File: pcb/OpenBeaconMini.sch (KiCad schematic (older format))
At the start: 47 parts, among them J1 *+12VDC, J2 *Ant, Q1 2N4401, Q2 2N4403, Q3 2N4401, Q4 2N7000, Q5 2N4401, U1 78L05, U2 ATTINY45-20PU, X1 CRYSTAL

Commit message: New OpenBeacon Mini for 2017
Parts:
- removed C13: 100n, symbol C
- removed C14, C15, C16: C, symbol C
- removed C2: 45, symbol CTRIM
- removed D1: Red, symbol LED
- removed J1: *+12VDC, symbol CONN_3
- removed J2: *Ant, symbol BNC
- removed L1: L, symbol L
- removed L3, L4: L-IRONCORE, symbol L-IRONCORE
- removed Q1, Q3, Q5: 2N4401, symbol NPN
- removed Q4: 2N7000, symbol MOSFET_N
- removed R11: 330, symbol R
- removed R12, R3: 150k, symbol R
- removed R13: 1k, symbol R
- removed R14: 4.7k, symbol R
- removed R15: 10, symbol R
- removed R16: 47, symbol R
- removed U1: 78L05, symbol VREG
- removed U2: ATTINY45-20PU, symbol ATTINY85
- removed X1: CRYSTAL, symbol CRYSTAL
- added C2: 100n, symbol C
- added J1: Bias V, symbol CONN_01X01
- added J2: PAI+, symbol CONN_01X01
- added J3: PAI-, symbol CONN_01X01
- added J4: Digital IO, symbol Conn_01x10
- added J5: SMA, symbol BNC
- added J6: I2C Bus, symbol Conn_01x04
- added J7: ADC Inputs, symbol Conn_01x10
- added J8: GND, symbol CONN_01X01
- added J9: BNC, symbol BNC
- added L1: FDSD0420-H-100M-P3, symbol L-IRONCORE
- added M1: LPFModule, symbol LPFModule
- added Q1: 2N7002, symbol MOS_N
- added Q3: RD00HVS1, symbol MOS_N
- added R3: PAT1220-C-10dB, symbol ChipAttenuator
- added S1: Left, symbol PUSHBUTTON_TACTILE
- added S2: Menu 1, symbol PUSHBUTTON_TACTILE
- added S3: Down, symbol PUSHBUTTON_TACTILE
- added S4: Up, symbol PUSHBUTTON_TACTILE
- added S5: Menu 2, symbol PUSHBUTTON_TACTILE
- added S6: Right, symbol PUSHBUTTON_TACTILE
- added S7: Back, symbol PUSHBUTTON_TACTILE
- added U1: TLV61046A, symbol TLV61046A
- added U2: ASTX-H11-25.000MHZ-T, symbol OSCILLATOR
- added U3: SN74LVC1G17, symbol SN74LVC1G17
- added U4: SI5351A, MODULE, symbol SI5351A
- added U5: MCP4725A1T-E/CH, symbol MCP4725A1T
- added U6: 128x32OLED, symbol 128x32OLED
- added U7: Empyrean, symbol Empyrean
- C1: value Gimmick -> 10n
- C3: value C -> 2.2u
- C4: value C -> 10u
- C7, C9: value 100n -> 1u
- L2: value FT37-43 10T -> FB2402-61 5T
- Q2: value 2N4403 -> MMBT4403
- R1, R2: value 10k -> 22k
- R10: value 22k -> 10k
- R4: value 47 -> 22k
- R5: value 2.2k -> 3.3k
- R6: value 150k -> 10
- R7: value 22k -> 56
- R8: value 1k -> 1 1%
- R9: value 150k -> 10k
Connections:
- net labels added: +3.3V, A1, A2, A3, A4, A5, BAND_ID, BTN_BACK, BTN_DOWN, BTN_DSP_1, BTN_DSP_2, BTN_LEFT, BTN_RIGHT, BTN_UP, CLK0, D10, D11, D7, D8, D9, SCL, SDA, TX
- net labels removed: +12V, FSK, Key, S1, S2, S3
- wire segments 88 -> 136
- no-connect marks 1 -> 8
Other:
- note added: "Boost Converter"
- note added: "Keying"
- note added: "Low-Pass Filter\nPlug-in Module"
- note added: "PA Bias"
- note added: "Power Amplifier"
- note added: "Si5351A PLL"
- note added: "User Interface"
- note removed: "Freq Trim"
- note removed: "Offset"
- note removed: "Starred components (*) are not included with kit"

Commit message: Add I2C level conversion
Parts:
- added J5: SMA, symbol BNC
- added Q4, Q5: 2N7002, symbol MOS_N
- added R10, R9: 10k, symbol R
- renumbered J9 to J10, J5 to J6, J6 to J7, J7 to J8, J8 to J9, R9 to R11, R10 to R12
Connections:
- net labels added: SCL_5V, SDA_5V
- wire segments 136 -> 146
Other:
- note added: "I2C Level Conversion"

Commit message: Add firmware to repo
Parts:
- C1, C10, C11, C12, C2, C3, C4, C5, C6, C7, C8, C9: footprint (none) -> EtherkitKicadLibrary:C_0805
- J1, J2, J3, J9: footprint (none) -> Measurement_Points:Measurement_Point_Square-TH_Small
- J10: footprint (none) -> EtherkitKicadLibrary:BNC-AMPHENOL-31-5431-10RFX
- J4, J8: footprint (none) -> Pin_Headers:Pin_Header_Straight_1x06_Pitch2.54mm; symbol Conn_01x10 -> Conn_01x06
- J5, J6: footprint (none) -> EtherkitKicadLibrary:SMA-ENDLAUNCH
- J7: footprint (none) -> Pin_Headers:Pin_Header_Straight_1x04_Pitch2.54mm
- L1: footprint (none) -> EtherkitKicadLibrary:Murata100M
- L2: footprint (none) -> EtherkitKicadLibrary:BN2402
- M1: footprint (none) -> EtherkitKicadLibrary:LPFModule
- Q1, Q4, Q5: footprint (none) -> EtherkitKicadLibrary:SOT23-2N7002
- Q2: footprint (none) -> EtherkitKicadLibrary:SOT23-MMBT440X
- Q3: footprint (none) -> EtherkitKicadLibrary:SOT89-3
- R1, R10, R11, R12, R2, R4, R5, R6, R7, R8, R9: footprint (none) -> EtherkitKicadLibrary:R_0805
- R3: footprint (none) -> EtherkitKicadLibrary:PAT1220
- S1, S2, S3, S4, S5, S6, S7: footprint (none) -> EtherkitKicadLibrary:Omron_B3F-1052
- U1, U5: footprint (none) -> EtherkitKicadLibrary:SOT23-6
- U2: footprint (none) -> EtherkitKicadLibrary:ASTX-H11-25.000MHZ-T
- U3: footprint (none) -> EtherkitKicadLibrary:SOT23-5
- U4: footprint MODULE -> EtherkitKicadLibrary:MSOP-10
- U6: footprint (none) -> EtherkitKicadLibrary:128x32OLED
- U7: footprint (none) -> EtherkitKicadLibrary:Empyrean
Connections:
- wire segments 146 -> 142

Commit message: New firmware and time sync software
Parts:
- R10, R11, R12, R9: value 10k -> 3.3k
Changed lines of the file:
@@
 Sheet 1 1
 Title "OpenBeacon Mini"
-Date "2017-12-02"
+Date "2018-04-10"
 Rev "A"
 Comp "Etherkit"
@@
 P 7500 4585
 F 0 "R12" H 7635 4625 50  0000 C CNN
-F 1 "10k" H 7630 4560 50  0000 C CNN
+F 1 "3.3k" H 7655 4555 50  0000 C CNN
 F 2 "EtherkitKicadLibrary:R_0805" H 7500 4585 60  0001 C CNN
 F 3 "" H 7500 4585 60  0000 C CNN
@@
 P 7180 4585
 F 0 "R11" H 7310 4625 50  0000 C CNN
-F 1 "10k" H 7315 4555 50  0000 C CNN
+F 1 "3.3k" H 7315 4555 50  0000 C CNN
 F 2 "EtherkitKicadLibrary:R_0805" H 7180 4585 60  0001 C CNN
 F 3 "" H 7180 4585 60  0000 C CNN
@@
 P 6090 5600
 F 0 "R10" H 6225 5645 50  0000 C CNN
-F 1 "10k" H 6225 5570 50  0000 C CNN
+F 1 "3.3k" H 6225 5570 50  0000 C CNN
 F 2 "EtherkitKicadLibrary:R_0805" H 6090 5600 60  0001 C CNN
 F 3 "" H 6090 5600 60  0000 C CNN
@@
 P 5790 5600
 F 0 "R9" H 5900 5640 50  0000 C CNN
-F 1 "10k" H 5925 5570 50  0000 C CNN
+F 1 "3.3k" H 5925 5570 50  0000 C CNN
 F 2 "EtherkitKicadLibrary:R_0805" H 5790 5600 60  0001 C CNN
 F 3 "" H 5790 5600 60  0000 C CNN

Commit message: Reimplement config storage, implement flash NVM
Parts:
- C1, C10, C11, C12, C2, C3, C4, C5, C6, C7, C8, C9: symbol C -> EtherkitKicadLibrary:C
- J1, J2, J3, J9: symbol CONN_01X01 -> EtherkitKicadLibrary:CONN_01X01
- J10, J5, J6: symbol BNC -> EtherkitKicadLibrary:BNC
- J4, J8: symbol Conn_01x06 -> OpenBeaconMini-rescue:Conn_01x06
- J7: symbol Conn_01x04 -> OpenBeaconMini-rescue:Conn_01x04
- L1, L2: symbol L-IRONCORE -> EtherkitKicadLibrary:L-IRONCORE
- M1: symbol LPFModule -> EtherkitKicadLibrary:LPFModule
- Q1, Q3, Q4, Q5: symbol MOS_N -> EtherkitKicadLibrary:MOS_N
- Q2: symbol PNP -> EtherkitKicadLibrary:PNP
- R1, R10, R11, R12, R2, R4, R5, R6, R7, R8, R9: symbol R -> EtherkitKicadLibrary:R
- R3: symbol ChipAttenuator -> EtherkitKicadLibrary:ChipAttenuator
- S1, S2, S3, S4, S5, S6, S7: symbol PUSHBUTTON_TACTILE -> EtherkitKicadLibrary:PUSHBUTTON_TACTILE
- U1: symbol TLV61046A -> EtherkitKicadLibrary:TLV61046A
- U2: symbol OSCILLATOR -> EtherkitKicadLibrary:OSCILLATOR
- U3: symbol SN74LVC1G17 -> EtherkitKicadLibrary:SN74LVC1G17
- U4: symbol SI5351A -> EtherkitKicadLibrary:SI5351A
- U5: symbol MCP4725A1T -> EtherkitKicadLibrary:MCP4725A1T
- U6: symbol 128x32OLED -> EtherkitKicadLibrary:128x32OLED
- U7: symbol Empyrean -> EtherkitKicadLibrary:Empyrean
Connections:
- wire segments 142 -> 188

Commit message: Initial schematic to Rev B
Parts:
- removed J4: Digital IO, Pin_Headers:Pin_Header_Straight_1x06_Pitch2.54mm, symbol OpenBeaconMini-rescue:Conn_01x06
- added C12, C13, C17: 100n, EtherkitKicadLibrary:C_0805, symbol EtherkitKicadLibrary:C
- added C15, C16: 4.7u, EtherkitKicadLibrary:C_0805, symbol EtherkitKicadLibrary:C
- added D1, D2: 1N4148W, Diode_SMD:D_SOD-123, symbol EtherkitKicadLibrary:DIODE
- added J10: UART, Pin_Headers:Pin_Header_Straight_1x04_Pitch2.54mm, symbol OpenBeaconMini-rescue:Conn_01x04
- added J4: Digital IO, Pin_Headers:Pin_Header_Straight_1x04_Pitch2.54mm, symbol OpenBeaconMini-rescue:Conn_01x04
- added K1, K2: G5V-1-DC5, Relay_THT:Relay_SPDT_Omron_G5V-1, symbol Relay:G5V-1
- added M2: LPF 2, EtherkitKicadLibrary:LPFModule, symbol EtherkitKicadLibrary:LPFModule
- added Q6: 2N7002, EtherkitKicadLibrary:SOT23-2N7002, symbol EtherkitKicadLibrary:MOS_N
- added R10, R9: 270k, EtherkitKicadLibrary:R_0805, symbol EtherkitKicadLibrary:R
- added R13: 22k, EtherkitKicadLibrary:R_0805, symbol EtherkitKicadLibrary:R
- added U8: 24AA64T, Package_TO_SOT_SMD:SOT-23-5, symbol EtherkitKicadLibrary:24AA64T
- M1: value LPFModule -> LPF 1
- Q3: value RD00HVS1 -> 2SK3074
- renumbered C2 to C1, C12 to C14, C3 to C2, C4 to C3, C1 to C4, J10 to J11, J8 to J5, J5 to J6, J6 to J7, J7 to J8, R9 to R11, R10 to R12, R11 to R14, R12 to R15, R4 to R2, R2 to R3, R3 to R4, S2 to S1, S5 to S2, S1 to S3, S3 to S4, S4 to S5, S7 to S6, S6 to S7
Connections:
- net BAND_ID is gone; now on net BAND_ID_1: U7.8 (A0)
- net D7 is gone; now on net BTN_LEFT: U7.21 (D7)
- net D8 is gone; now on net BTN_DSP_1: U7.22 (D8)
- net D9 is gone; now on net BTN_DSP_2: U7.23 (D9)
- net +3.3V: now also M1.9 (VCC), C15.1, C16.1, C17.1, J10.1 (Pin_1), M2.9 (VCC), U8.4 (VCC); no longer M1.8 (GND)
- net +5V: now also D1.2 (K), D2.2 (K), K1.2, K2.2
- net A2: now also J5.1 (Pin_1); no longer J5.3 (Pin_3)
- net A3: now also J5.3 (Pin_3); no longer J5.5 (Pin_5)
- net A4: now also J5.5 (Pin_5)
- net BTN_DSP_1: no longer U7.14 (D0)
- net BTN_DSP_2: no longer U7.15 (D1)
- net BTN_LEFT: no longer U7.18 (D4)
- net D10: now also J4.3 (Pin_3)
- net GND: now also M1.1 (GND), M1.3 (GND), M1.5 (GND), M1.8 (GND), C12.2, C13.2, C15.2, C16.2, C17.2, J10.4 (Pin_4), J4.2 (Pin_2), J4.4 (Pin_4), M2.1 (GND), M2.3 (GND), M2.5 (GND), M2.6 (GND), M2.8 (GND), Q6.1 (S), R10.2, R13.2, R9.2, U8.2 (VSS), U8.5 (WP); no longer M1.9 (VCC)
- net SCL: now also U8.1 (SCL)
- net SDA: now also U8.3 (SDA)
- net TX: now also U7.26 (D12); no longer U7.27 (D13)
- net at C11.1: now also K1.5, K1.6
- net BAND_ID_1: now reaches M1.2 (BAND_V)
- net BAND_ID_1: now also C12.1, R9.1
- net at M1.4 (RF): now also K1.1
- net at M1.7 (RF): now also K2.1; no longer J11.1 (In)
- net at C3.1, Q2.1 (E), U1.5 (VO): now also R2.1; no longer C4.1
- net at Q2.3 (C), R6.2: now also C4.1; no longer R2.1
- net A1 renamed BAND_ID_2
- net BAND_ID_2: now also C13.1, M2.2 (BAND_V), R10.1; no longer J5.1 (Pin_1)
- net A5: no longer names the net of U7.13 (A5)
- net D11 renamed BAND_SW
- net BAND_SW: now also Q6.2 (G), R13.1
- new net: J11.1 (In), K2.5, K2.6
- new net: K1.10, M2.4 (RF)
- new net: K2.10, M2.7 (RF)
- new net BAND_RELAY: D1.1 (A), D2.1 (A), K1.9, K2.9, Q6.3 (D)
- new net D4: J4.1 (Pin_1), U7.18 (D4)
- new net UART_RX: J10.2 (Pin_2), U7.14 (D0)
- new net UART_TX: J10.3 (Pin_3), U7.15 (D1)
- no-connect marks 8 -> 9
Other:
- note added: "External EEPROM"
- note added: "IO Headers"
- note added: "Low-Pass Filter\nPlug-in Modules"
- note removed: "Low-Pass Filter\nPlug-in Module"
- moved on the sheet: C4, J11, J5, J8, M1, Q4, Q5, R11, R12, R14, R15, R2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

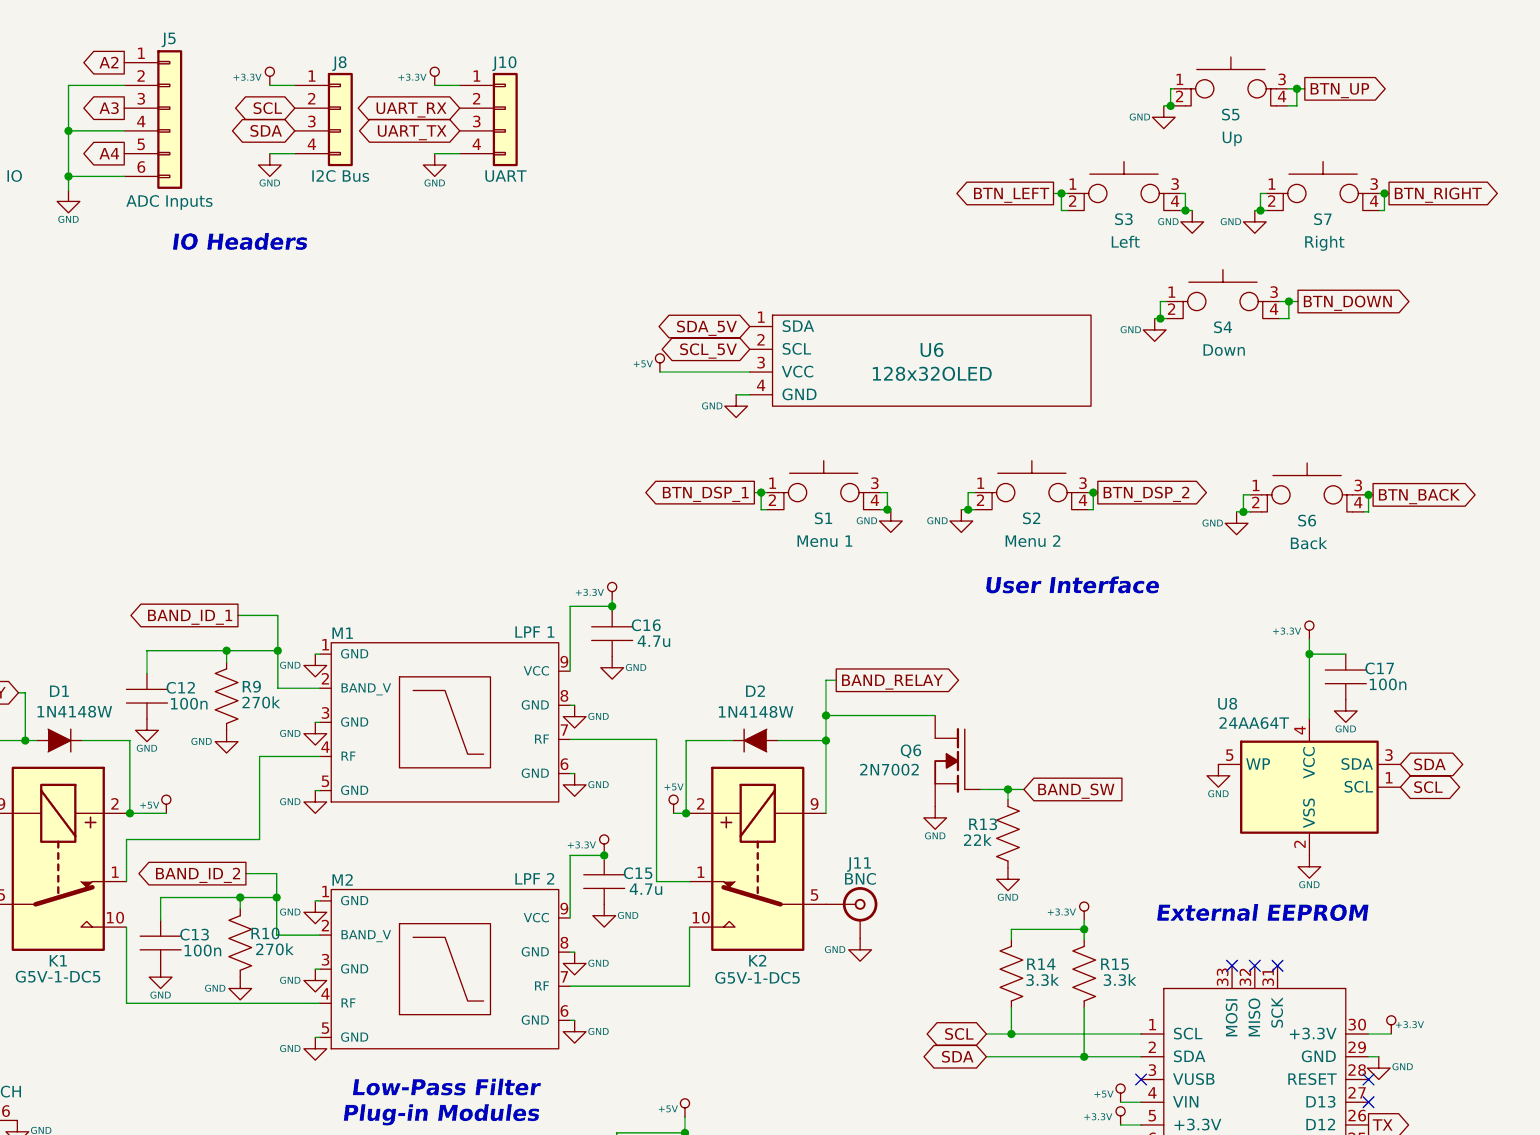
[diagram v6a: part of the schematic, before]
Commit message: Add debounce caps to buttons
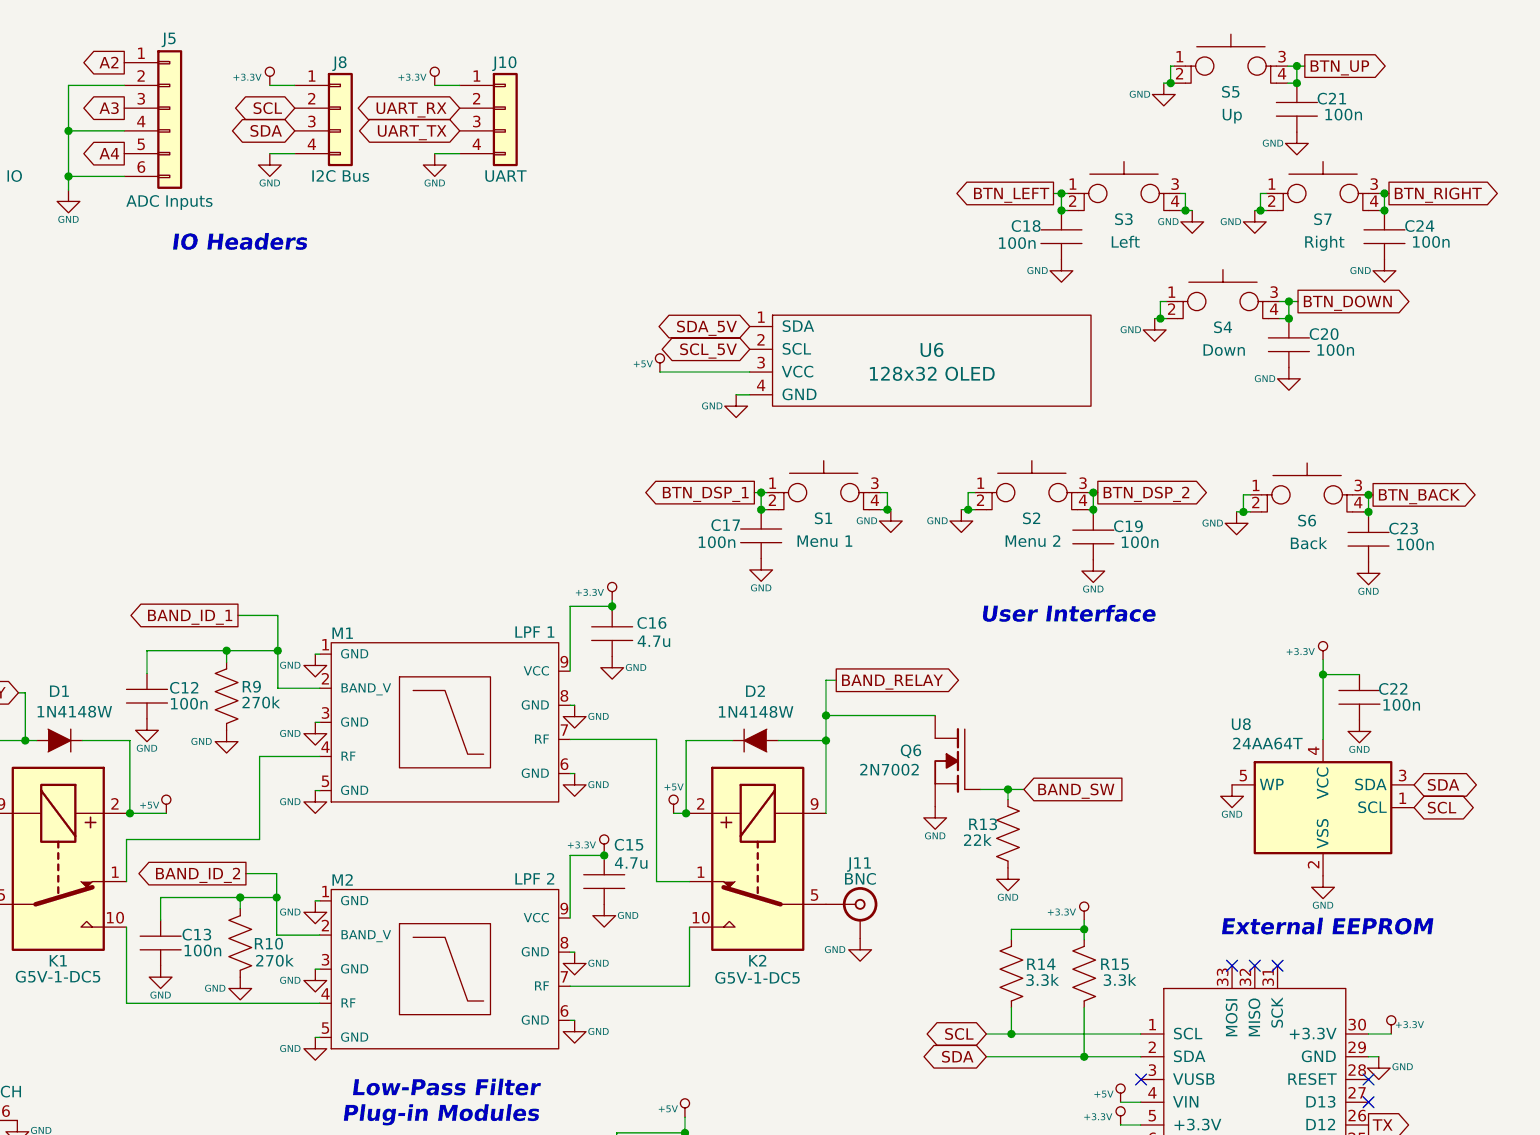
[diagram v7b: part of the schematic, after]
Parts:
- added C17, C18, C19, C20, C21, C23, C24: 100n, Capacitor_SMD:C_0805_2012Metric, symbol EtherkitKicadLibrary:C
- C1, C10, C11, C12, C13, C14, C15, C16, C2, C3, C4, C5, C6, C7, C8, C9: footprint EtherkitKicadLibrary:C_0805 -> Capacitor_SMD:C_0805_2012Metric
- C22: renamed from C17; footprint EtherkitKicadLibrary:C_0805 -> Capacitor_SMD:C_0805_2012Metric
- R1, R10, R11, R12, R13, R14, R15, R2, R3, R5, R6, R7, R8, R9: footprint EtherkitKicadLibrary:R_0805 -> Resistor_SMD:R_0805_2012Metric
- U6: value 128x32OLED -> 128x32 OLED
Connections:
- net BTN_BACK: now also C23.1
- net BTN_DOWN: now also C20.1
- net BTN_DSP_1: now also C17.1
- net BTN_DSP_2: now also C19.1
- net BTN_LEFT: now also C18.1
- net BTN_RIGHT: now also C24.1
- net BTN_UP: now also C21.1
- net GND: now also C17.2, C18.2, C19.2, C20.2, C21.2, C23.2, C24.2
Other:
- moved on the sheet: C22, S5, U8
